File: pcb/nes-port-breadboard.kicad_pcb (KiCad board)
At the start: 2 copper layers, 35.6 x 35.6 mm, 4 parts, among them J1 NES_Port_Male, J2 Conn_01x07

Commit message: Tweak bottom silk. Prep for Gerbers.
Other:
- board text added: "Ver. 1.0.1"
- board text removed: "Version 1.0.1"
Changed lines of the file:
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@@
       (psa4output false)
       (plotreference true)
-      (plotvalue true)
+      (plotvalue false)
       (plotinvisibletext false)
       (padsonsilk false)
@@
     (pad 1 np_thru_hole circle (at 0 0) (size 2.7 2.7) (drill 2.7) (layers *.Cu *.Mask))
   )
-  (gr_text "Dave Dribin" (at 160.02 93.472) (layer F.SilkS)
-    (effects (font (size 1 1) (thickness 0.15)) (justify right))
+  (gr_text "Dave Dribin" (at 152.4 93.472) (layer F.SilkS)
+    (effects (font (size 1 1) (thickness 0.15)) (justify left))
   )
   (gr_line (start 123.19 127) (end 123.19 127) (layer Edge.Cuts) (width 0.0254))
@@
     (arrow2b (pts (xy 165.735 90.17) (xy 166.321421 91.296504)))
   )
-  (gr_text "Version 1.0.1" (at 160.02 93.472) (layer B.SilkS)
+  (gr_text "Ver. 1.0.1" (at 160.02 93.345) (layer B.SilkS)
     (effects (font (size 1 1) (thickness 0.15)) (justify left mirror))
   )

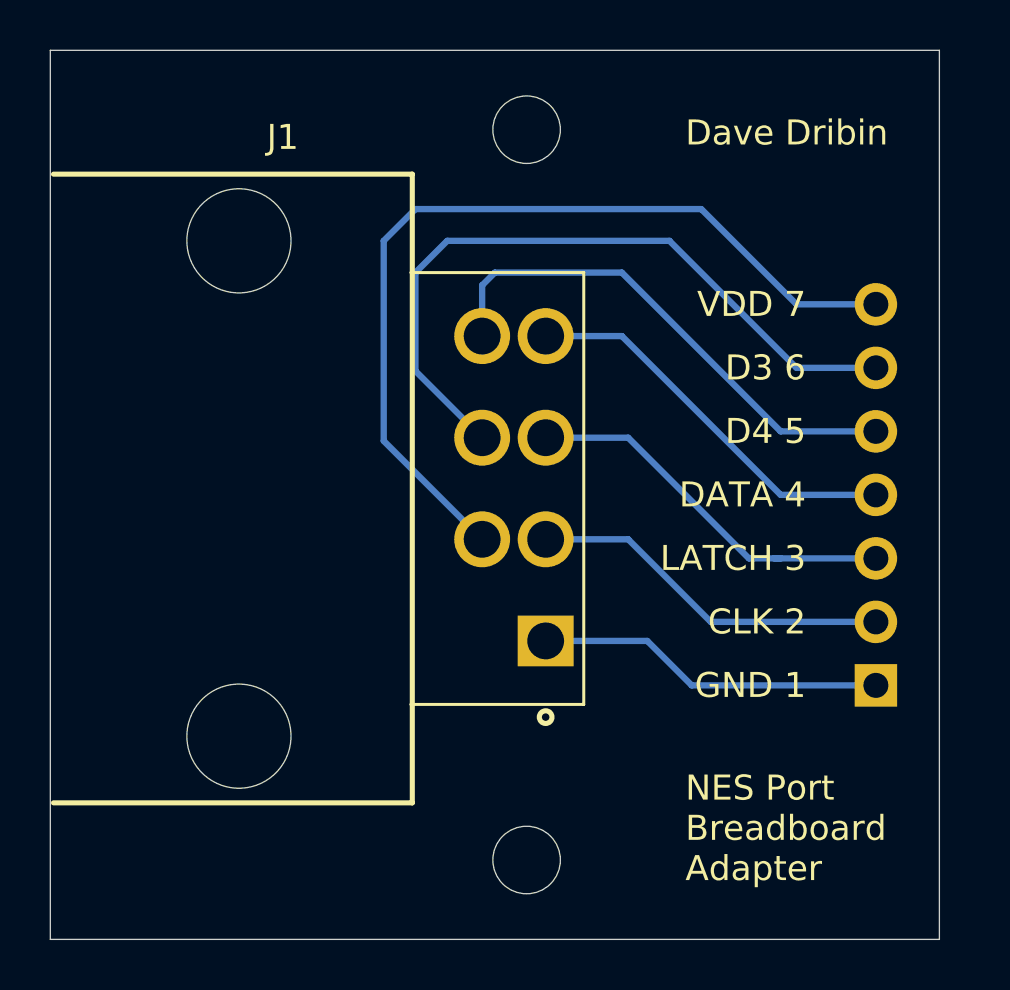
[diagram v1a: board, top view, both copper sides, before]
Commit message: Center NES port vertically
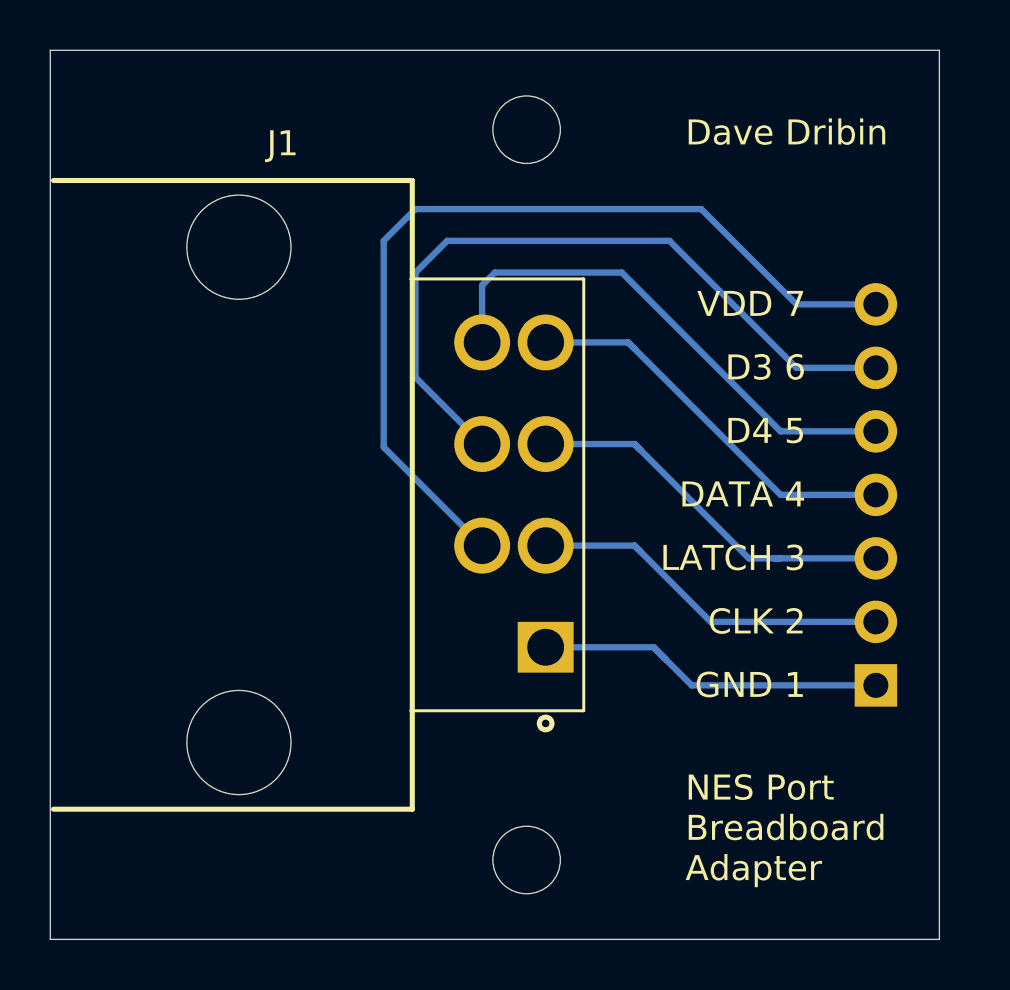
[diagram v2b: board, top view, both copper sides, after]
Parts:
- moved J1 0.25 mm to (147.6, 108.0)
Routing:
- net Net-(J1-Pad1): track 13.9 -> 14.6 mm

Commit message: Update schematic symbol for NES port
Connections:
- net Net-(J1-Pad1) renamed /GND
- net Net-(J1-Pad2) renamed /CLK
- net Net-(J1-Pad3) renamed /LATCH
- net Net-(J1-Pad4) renamed /DATA
- net Net-(J1-Pad5) renamed /D4
- net Net-(J1-Pad6) renamed /D3
- net Net-(J1-Pad7) renamed /VDD
